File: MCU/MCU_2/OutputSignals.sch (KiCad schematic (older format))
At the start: 29 parts, among them J11 Conn_01x02, J12 Conn_01x02, J13 Conn_01x02, Q2 8050, Q3 8050, Q4 8550, Q5 8050, U11 PC817, U9 ICL7660

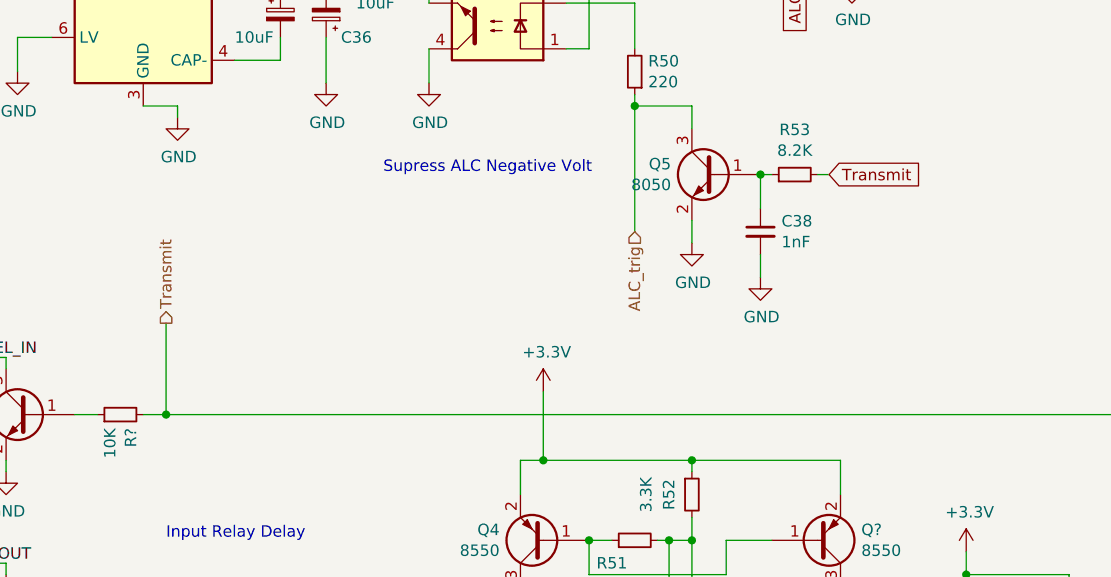
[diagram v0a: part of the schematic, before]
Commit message: OPA1000 and 2000 compatibility
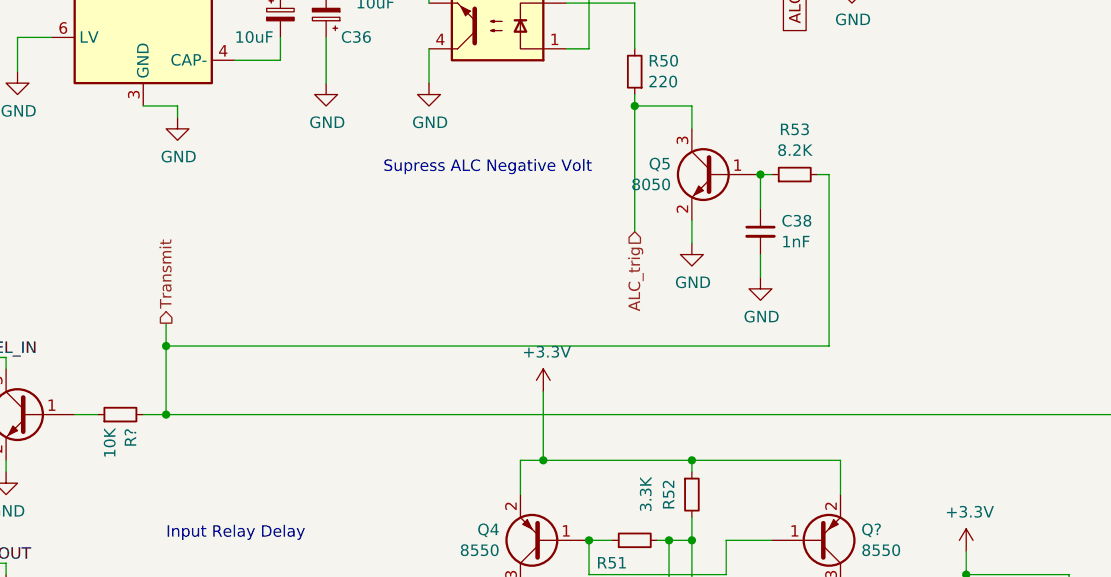
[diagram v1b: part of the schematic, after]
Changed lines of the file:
@@
 EESchema Schematic File Version 4
-LIBS:MCU-cache
 EELAYER 30 0
 EELAYER END
@@
 $EndComp
 Wire Wire Line
-	2850 2850 2850 3250
+	2850 2850 2850 2950
 Wire Wire Line
 	2450 4150 2550 4150
@@
 Wire Wire Line
 	5500 2200 5450 2200
-Text GLabel 5750 2200 2    50   Input ~ 0
-Transmit
 Wire Wire Line
 	5750 2200 5700 2200
@@
 	1    0    0    -1
 $EndComp
+Connection ~ 2850 2950
+Wire Wire Line
+	2850 2950 2850 3250
+Wire Wire Line
+	5750 2200 5750 2950
+Wire Wire Line
+	2850 2950 5750 2950
 $EndSCHEMATC
